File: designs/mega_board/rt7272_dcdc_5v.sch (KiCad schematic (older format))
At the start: 13 parts

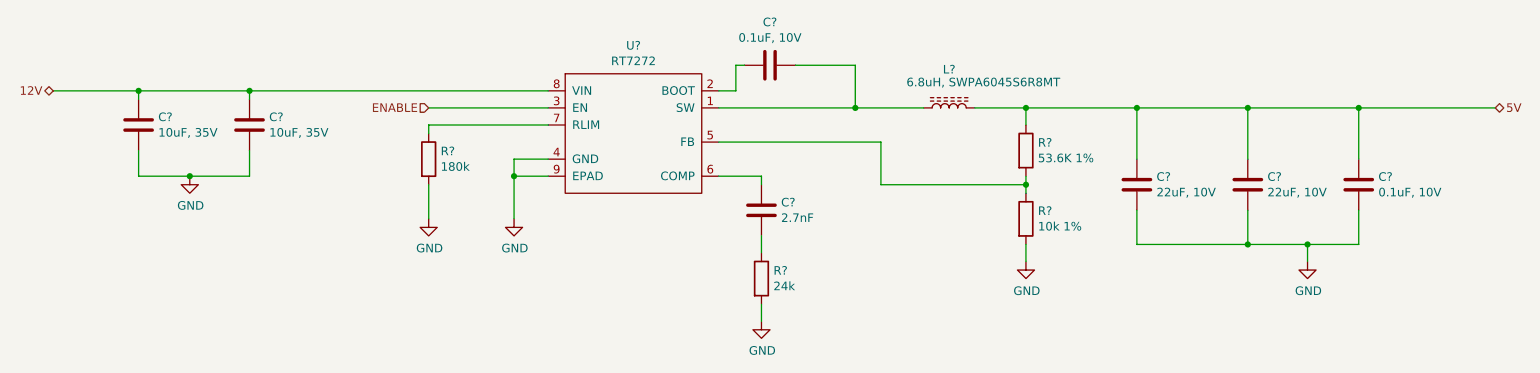
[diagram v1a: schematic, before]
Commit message: Enumerate components as is in eagle design.
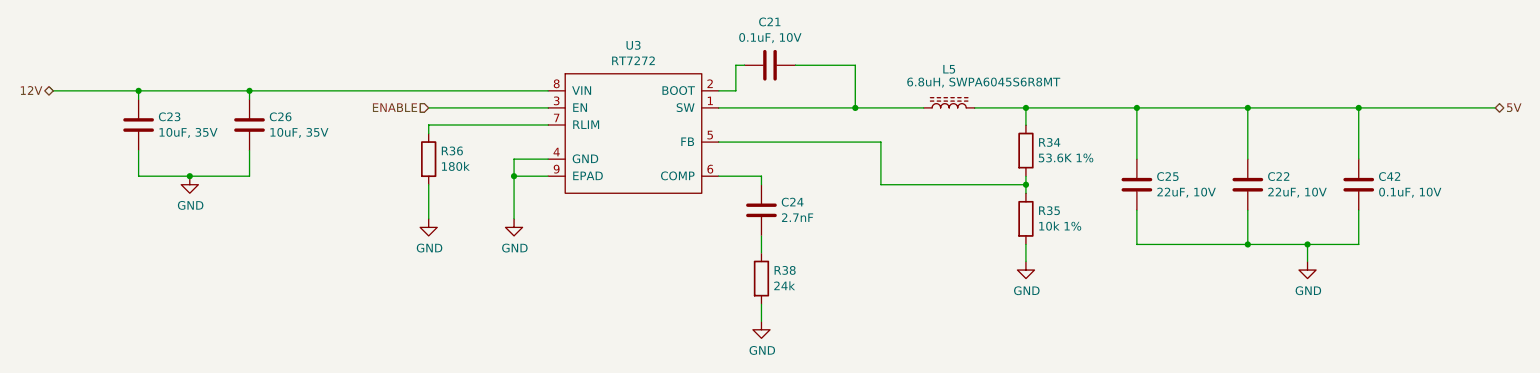
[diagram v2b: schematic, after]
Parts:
- C21, C24, C42: renamed from C?; footprint (none) -> LibreRouter_MegaBoard:C0402
- C22, C23, C25, C26: renamed from C?; footprint (none) -> LibreRouter_MegaBoard:C0805
- L5: renamed from L?; footprint (none) -> LibreRouter_MegaBoard:SWPA6028S
- R34, R35, R36, R38: renamed from R?; footprint (none) -> LibreRouter_MegaBoard:R0402
- U3: renamed from U?; footprint (none) -> LibreRouter_MegaBoard:RT8250-SOP8

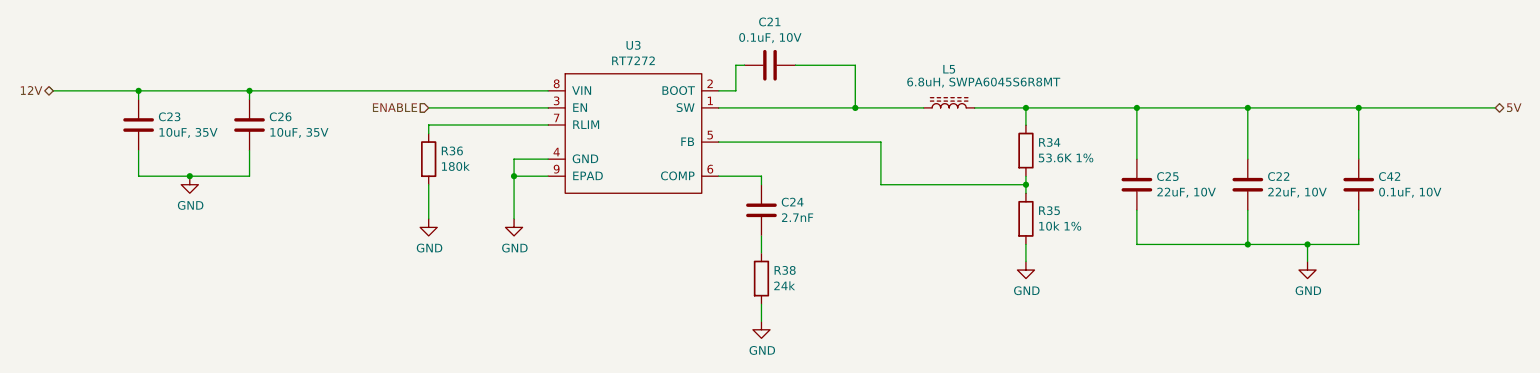
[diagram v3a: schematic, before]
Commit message: Add capacitor definito to BOM
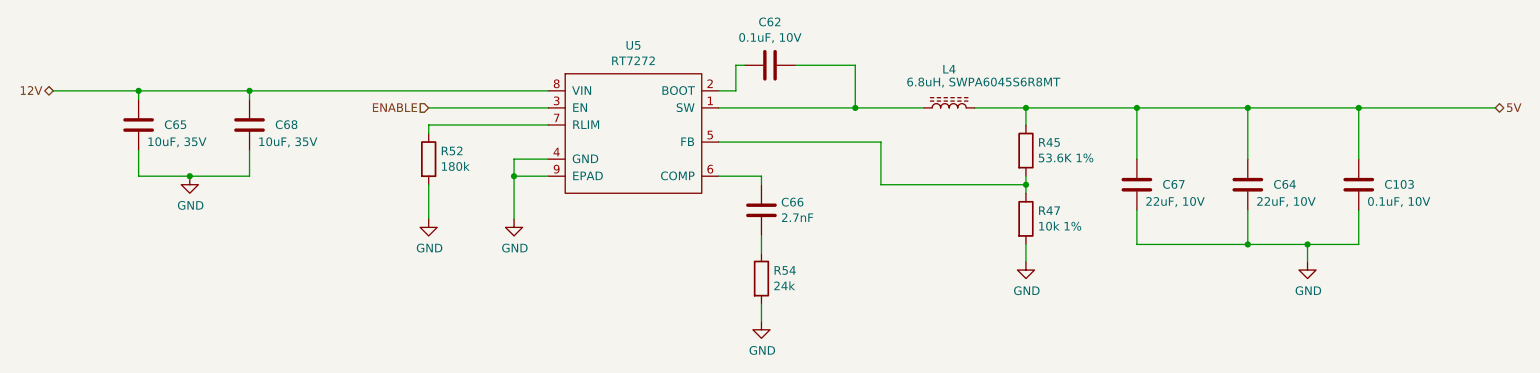
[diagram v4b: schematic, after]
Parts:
- C21, C42: Manufacturer (none) -> Murata Electronics; Manufacturer PN (none) -> GCM155R71A104KA55D; Supplier (none) -> DigiKey; Supplier PN (none) -> 490-16434-6-ND
- C22, C25: Manufacturer (none) -> Murata Electronics; Manufacturer PN (none) -> GRM21BR61A226ME51L; Supplier (none) -> DigiKey; Supplier PN (none) -> 490-10511-6-ND
- C23, C26: Manufacturer (none) -> Murata Electronics; Manufacturer PN (none) -> GRM21BR6YA106ME43L; Supplier (none) -> DigiKey; Supplier PN (none) -> 490-10515-6-ND
- C24: Manufacturer (none) -> Murata Electronics; Manufacturer PN (none) -> GRM1557U1A272JA01D; Supplier (none) -> DigiKey; Supplier PN (none) -> 490-6275-6-ND
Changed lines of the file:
@@
 $Descr A4 11693 8268
 encoding utf-8
-Sheet 7 14
+Sheet 9 14
 Title ""
 Date ""
@@
 AR Path="/5D0328DE/5D4FEB2F/5D42D1B4" Ref="U5"  Part="1"
 AR Path="/5D42D1B4" Ref="U?"  Part="1"
-F 0 "U3" H 5050 4115 50  0000 C CNN
+F 0 "U5" H 5050 4115 50  0000 C CNN
 F 1 "RT7272" H 5050 4024 50  0000 C CNN
 F 2 "LibreRouter_MegaBoard:RT8250-SOP8" H 5050 3600 50  0001 C CNN
@@
 AR Path="/5D0328DE/5D4FE12B/5D42D229" Ref="C53"  Part="1"
 AR Path="/5D0328DE/5D4FEB2F/5D42D229" Ref="C68"  Part="1"
-F 0 "C26" H 2915 3596 50  0000 L CNN
-F 1 "10uF, 35V" H 2915 3505 50  0000 L CNN
+F 0 "C68" H 2950 3550 50  0000 L CNN
+F 1 "10uF, 35V" H 2850 3450 50  0000 L CNN
 F 2 "LibreRouter_MegaBoard:C0805" H 2838 3400 50  0001 C CNN
 F 3 "~" H 2800 3550 50  0001 C CNN
+F 4 "DigiKey" H 2800 3550 50  0001 C CNN "Supplier"
+F 5 "Murata Electronics" H 2800 3550 50  0001 C CNN "Manufacturer"
+F 6 "GRM21BR6YA106ME43L" H 2800 3550 50  0001 C CNN "Manufacturer PN"
+F 7 "490-10515-6-ND" H 2800 3550 50  0001 C CNN "Supplier PN"
 	1    2800 3550
 	1    0    0    -1
@@
 AR Path="/5D0328DE/5D4FE12B/5D42D2DE" Ref="R13"  Part="1"
 AR Path="/5D0328DE/5D4FEB2F/5D42D2DE" Ref="R52"  Part="1"
-F 0 "R36" H 3920 3796 50  0000 L CNN
+F 0 "R52" H 3920 3796 50  0000 L CNN
 F 1 "180k" H 3920 3705 50  0000 L CNN
 F 2 "LibreRouter_MegaBoard:R0402" V 3780 3750 50  0001 C CNN
@@
 AR Path="/5D0328DE/5D4FE12B/5D42D3B9" Ref="L3"  Part="1"
 AR Path="/5D0328DE/5D4FEB2F/5D42D3B9" Ref="L4"  Part="1"
-F 0 "L5" V 7125 3450 50  0000 C CNN
+F 0 "L4" V 7125 3450 50  0000 C CNN
 F 1 "6.8uH, SWPA6045S6R8MT" V 7050 3250 50  0000 C CNN
 F 2 "LibreRouter_MegaBoard:SWPA6028S" H 6900 3450 50  0001 C CNN
@@
 AR Path="/5D0328DE/5D4FE12B/5D42D488" Ref="C30"  Part="1"
 AR Path="/5D0328DE/5D4FEB2F/5D42D488" Ref="C62"  Part="1"
-F 0 "C21" V 5598 3200 50  0000 C CNN
+F 0 "C62" V 5598 3200 50  0000 C CNN
 F 1 "0.1uF, 10V" V 5689 3200 50  0000 C CNN
 F 2 "LibreRouter_MegaBoard:C0402" H 5888 3050 50  0001 C CNN
 F 3 "~" H 5850 3200 50  0001 C CNN
+F 4 "Murata Electronics" H 5850 3200 50  0001 C CNN "Manufacturer"
+F 5 "GCM155R71A104KA55D" H 5850 3200 50  0001 C CNN "Manufacturer PN"
+F 6 "DigiKey" H 5850 3200 50  0001 C CNN "Supplier"
+F 7 "490-16434-6-ND" H 5850 3200 50  0001 C CNN "Supplier PN"
 	1    5850 3200
 	0    1    1    0
@@
 AR Path="/5D0328DE/5D4FE12B/5D42D571" Ref="R10"  Part="1"
 AR Path="/5D0328DE/5D4FEB2F/5D42D571" Ref="R45"  Part="1"
-F 0 "R34" H 7420 3746 50  0000 L CNN
+F 0 "R45" H 7420 3746 50  0000 L CNN
 F 1 "53.6K 1%" H 7420 3655 50  0000 L CNN
 F 2 "LibreRouter_MegaBoard:R0402" V 7280 3700 50  0001 C CNN
@@
 AR Path="/5D0328DE/5D4FE12B/5D42D5CB" Ref="R12"  Part="1"
 AR Path="/5D0328DE/5D4FEB2F/5D42D5CB" Ref="R47"  Part="1"
-F 0 "R35" H 7420 4146 50  0000 L CNN
+F 0 "R47" H 7420 4146 50  0000 L CNN
 F 1 "10k 1%" H 7420 4055 50  0000 L CNN
 F 2 "LibreRouter_MegaBoard:R0402" V 7280 4100 50  0001 C CNN
@@
 AR Path="/5D0328DE/5D4FE12B/5D42D605" Ref="R16"  Part="1"
 AR Path="/5D0328DE/5D4FEB2F/5D42D605" Ref="R54"  Part="1"
-F 0 "R38" H 5870 4496 50  0000 L CNN
+F 0 "R54" H 5870 4496 50  0000 L CNN
 F 1 "24k" H 5870 4405 50  0000 L CNN
 F 2 "LibreRouter_MegaBoard:R0402" V 5730 4450 50  0001 C CNN
@@
 AR Path="/5D0328DE/5D4FE12B/5D42D659" Ref="C45"  Part="1"
 AR Path="/5D0328DE/5D4FEB2F/5D42D659" Ref="C66"  Part="1"
-F 0 "C24" H 5685 4004 50  0000 R CNN
+F 0 "C66" H 5685 4004 50  0000 R CNN
 F 1 "2.7nF" H 5685 4095 50  0000 R CNN
 F 2 "LibreRouter_MegaBoard:C0402" H 5838 3900 50  0001 C CNN
 F 3 "~" H 5800 4050 50  0001 C CNN
+F 4 "DigiKey" H 5800 4050 50  0001 C CNN "Supplier"
+F 5 "GRM1557U1A272JA01D" H 5800 4050 50  0001 C CNN "Manufacturer PN"
+F 6 "490-6275-6-ND" H 5800 4050 50  0001 C CNN "Supplier PN"
+F 7 "Murata Electronics" H 5800 4050 50  0001 C CNN "Manufacturer"
 	1    5800 4050
 	-1   0    0    1
@@
 AR Path="/5D0328DE/5D4FE12B/5D42DAC0" Ref="C46"  Part="1"
 AR Path="/5D0328DE/5D4FEB2F/5D42DAC0" Ref="C67"  Part="1"
-F 0 "C25" H 7885 3854 50  0000 R CNN
-F 1 "22uF, 10V" H 7885 3945 50  0000 R CNN
+F 0 "C67" H 7850 3900 50  0000 R CNN
+F 1 "22uF, 10V" H 7950 4000 50  0000 R CNN
 F 2 "LibreRouter_MegaBoard:C0805" H 8038 3750 50  0001 C CNN
 F 3 "~" H 8000 3900 50  0001 C CNN
+F 4 "DigiKey" H 8000 3900 50  0001 C CNN "Supplier"
+F 5 "GRM21BR61A226ME51L" H 8000 3900 50  0001 C CNN "Manufacturer PN"
+F 6 "490-10511-6-ND" H 8000 3900 50  0001 C CNN "Supplier PN"
+F 7 "Murata Electronics" H 8000 3900 50  0001 C CNN "Manufacturer"
 	1    8000 3900
 	-1   0    0    1
@@
 AR Path="/5D0328DE/5D4FE12B/5D42DBCD" Ref="C31"  Part="1"
 AR Path="/5D0328DE/5D4FEB2F/5D42DBCD" Ref="C64"  Part="1"
-F 0 "C22" H 8535 3854 50  0000 R CNN
-F 1 "22uF, 10V" H 8535 3945 50  0000 R CNN
+F 0 "C64" H 8500 3900 50  0000 R CNN
+F 1 "22uF, 10V" H 8600 4000 50  0000 R CNN
 F 2 "LibreRouter_MegaBoard:C0805" H 8688 3750 50  0001 C CNN
 F 3 "~" H 8650 3900 50  0001 C CNN
+F 4 "DigiKey" H 8650 3900 50  0001 C CNN "Supplier"
+F 5 "GRM21BR61A226ME51L" H 8650 3900 50  0001 C CNN "Manufacturer PN"
+F 6 "490-10511-6-ND" H 8650 3900 50  0001 C CNN "Supplier PN"
+F 7 "Murata Electronics" H 8650 3900 50  0001 C CNN "Manufacturer"
 	1    8650 3900
 	-1   0    0    1
@@
 AR Path="/5D0328DE/5D4FE12B/5D42DC2B" Ref="C102"  Part="1"
 AR Path="/5D0328DE/5D4FEB2F/5D42DC2B" Ref="C103"  Part="1"
-F 0 "C42" H 9185 3854 50  0000 R CNN
-F 1 "0.1uF, 10V" H 9185 3945 50  0000 R CNN
+F 0 "C103" H 9150 3900 50  0000 R CNN
+F 1 "0.1uF, 10V" H 9250 4000 50  0000 R CNN
 F 2 "LibreRouter_MegaBoard:C0402" H 9338 3750 50  0001 C CNN
 F 3 "~" H 9300 3900 50  0001 C CNN
+F 4 "Murata Electronics" H 9300 3900 50  0001 C CNN "Manufacturer"
+F 5 "GCM155R71A104KA55D" H 9300 3900 50  0001 C CNN "Manufacturer PN"
+F 6 "DigiKey" H 9300 3900 50  0001 C CNN "Supplier"
+F 7 "490-16434-6-ND" H 9300 3900 50  0001 C CNN "Supplier PN"
 	1    9300 3900
 	-1   0    0    1
@@
 AR Path="/5D0328DE/5D4FE12B/5D43058C" Ref="C44"  Part="1"
 AR Path="/5D0328DE/5D4FEB2F/5D43058C" Ref="C65"  Part="1"
-F 0 "C23" H 2265 3596 50  0000 L CNN
-F 1 "10uF, 35V" H 2265 3505 50  0000 L CNN
+F 0 "C65" H 2300 3550 50  0000 L CNN
+F 1 "10uF, 35V" H 2200 3450 50  0000 L CNN
 F 2 "LibreRouter_MegaBoard:C0805" H 2188 3400 50  0001 C CNN
 F 3 "~" H 2150 3550 50  0001 C CNN
+F 4 "DigiKey" H 2150 3550 50  0001 C CNN "Supplier"
+F 5 "Murata Electronics" H 2150 3550 50  0001 C CNN "Manufacturer"
+F 6 "GRM21BR6YA106ME43L" H 2150 3550 50  0001 C CNN "Manufacturer PN"
+F 7 "490-10515-6-ND" H 2150 3550 50  0001 C CNN "Supplier PN"
 	1    2150 3550
 	1    0    0    -1

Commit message: Add BOM definition to all resistors
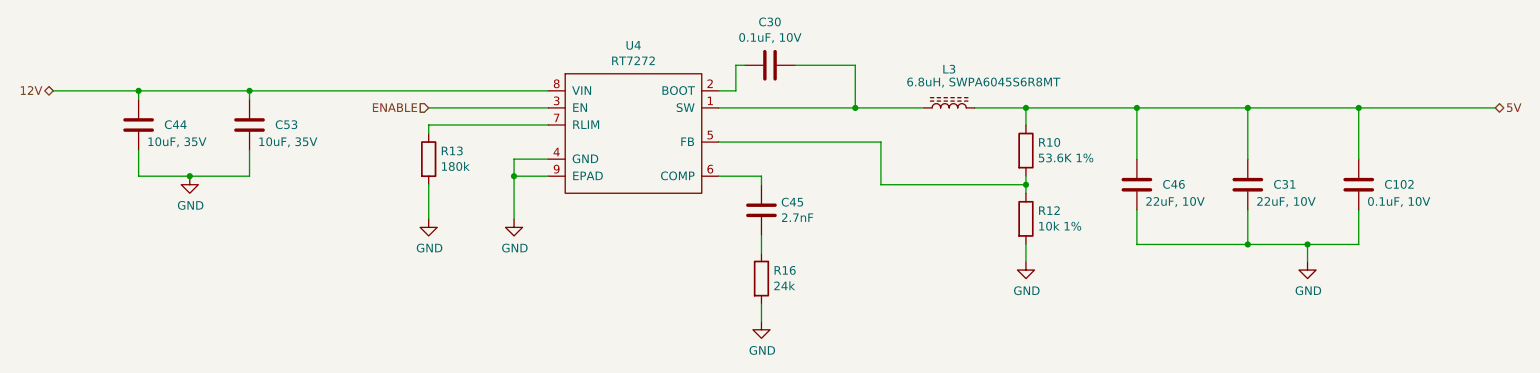
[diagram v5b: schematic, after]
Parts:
- R34: Manufacturer (none) -> Panasonic Electronic Components; Manufacturer PN (none) -> ERJ-2RKF5362X; Supplier (none) -> DigiKey; Supplier PN (none) -> P53.6KLDKR-ND
- R35: Manufacturer (none) -> Panasonic Electronic Components; Manufacturer PN (none) -> ERJ-PA2F1002X; Supplier (none) -> DigiKey; Supplier PN (none) -> P17230DKR-ND
- R36: Manufacturer (none) -> Panasonic Electronic Components; Manufacturer PN (none) -> ERJ-PA2F1803X; Supplier (none) -> DigiKey; Supplier PN (none) -> P124450DKR-ND
- R38: Manufacturer (none) -> Panasonic Electronic Components; Manufacturer PN (none) -> ERJ-PA2F2402X; Supplier (none) -> DigiKey; Supplier PN (none) -> P124459DKR-ND
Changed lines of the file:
@@
 $Descr A4 11693 8268
 encoding utf-8
-Sheet 9 14
+Sheet 8 14
 Title ""
 Date ""
@@
 AR Path="/5D0328DE/5D4FEB2F/5D42D1B4" Ref="U5"  Part="1"
 AR Path="/5D42D1B4" Ref="U?"  Part="1"
-F 0 "U5" H 5050 4115 50  0000 C CNN
+F 0 "U4" H 5050 4115 50  0000 C CNN
 F 1 "RT7272" H 5050 4024 50  0000 C CNN
 F 2 "LibreRouter_MegaBoard:RT8250-SOP8" H 5050 3600 50  0001 C CNN
@@
 AR Path="/5D0328DE/5D4FE12B/5D42D229" Ref="C53"  Part="1"
 AR Path="/5D0328DE/5D4FEB2F/5D42D229" Ref="C68"  Part="1"
-F 0 "C68" H 2950 3550 50  0000 L CNN
+F 0 "C53" H 2950 3550 50  0000 L CNN
 F 1 "10uF, 35V" H 2850 3450 50  0000 L CNN
 F 2 "LibreRouter_MegaBoard:C0805" H 2838 3400 50  0001 C CNN
@@
 AR Path="/5D0328DE/5D4FE12B/5D42D2DE" Ref="R13"  Part="1"
 AR Path="/5D0328DE/5D4FEB2F/5D42D2DE" Ref="R52"  Part="1"
-F 0 "R52" H 3920 3796 50  0000 L CNN
+F 0 "R13" H 3920 3796 50  0000 L CNN
 F 1 "180k" H 3920 3705 50  0000 L CNN
 F 2 "LibreRouter_MegaBoard:R0402" V 3780 3750 50  0001 C CNN
 F 3 "~" H 3850 3750 50  0001 C CNN
+F 4 "Panasonic Electronic Components" H 3850 3750 50  0001 C CNN "Manufacturer"
+F 5 "ERJ-PA2F1803X" H 3850 3750 50  0001 C CNN "Manufacturer PN"
+F 6 "DigiKey" H 3850 3750 50  0001 C CNN "Supplier"
+F 7 "P124450DKR-ND" H 3850 3750 50  0001 C CNN "Supplier PN"
 	1    3850 3750
 	1    0    0    -1
@@
 AR Path="/5D0328DE/5D4FE12B/5D42D3B9" Ref="L3"  Part="1"
 AR Path="/5D0328DE/5D4FEB2F/5D42D3B9" Ref="L4"  Part="1"
-F 0 "L4" V 7125 3450 50  0000 C CNN
+F 0 "L3" V 7125 3450 50  0000 C CNN
 F 1 "6.8uH, SWPA6045S6R8MT" V 7050 3250 50  0000 C CNN
 F 2 "LibreRouter_MegaBoard:SWPA6028S" H 6900 3450 50  0001 C CNN
@@
 AR Path="/5D0328DE/5D4FE12B/5D42D488" Ref="C30"  Part="1"
 AR Path="/5D0328DE/5D4FEB2F/5D42D488" Ref="C62"  Part="1"
-F 0 "C62" V 5598 3200 50  0000 C CNN
+F 0 "C30" V 5598 3200 50  0000 C CNN
 F 1 "0.1uF, 10V" V 5689 3200 50  0000 C CNN
 F 2 "LibreRouter_MegaBoard:C0402" H 5888 3050 50  0001 C CNN
@@
 AR Path="/5D0328DE/5D4FE12B/5D42D571" Ref="R10"  Part="1"
 AR Path="/5D0328DE/5D4FEB2F/5D42D571" Ref="R45"  Part="1"
-F 0 "R45" H 7420 3746 50  0000 L CNN
+F 0 "R10" H 7420 3746 50  0000 L CNN
 F 1 "53.6K 1%" H 7420 3655 50  0000 L CNN
 F 2 "LibreRouter_MegaBoard:R0402" V 7280 3700 50  0001 C CNN
 F 3 "~" H 7350 3700 50  0001 C CNN
+F 4 "Panasonic Electronic Components" H 7350 3700 50  0001 C CNN "Manufacturer"
+F 5 "ERJ-2RKF5362X" H 7350 3700 50  0001 C CNN "Manufacturer PN"
+F 6 "DigiKey" H 7350 3700 50  0001 C CNN "Supplier"
+F 7 "P53.6KLDKR-ND" H 7350 3700 50  0001 C CNN "Supplier PN"
 	1    7350 3700
 	1    0    0    -1
@@
 AR Path="/5D0328DE/5D4FE12B/5D42D5CB" Ref="R12"  Part="1"
 AR Path="/5D0328DE/5D4FEB2F/5D42D5CB" Ref="R47"  Part="1"
-F 0 "R47" H 7420 4146 50  0000 L CNN
+F 0 "R12" H 7420 4146 50  0000 L CNN
 F 1 "10k 1%" H 7420 4055 50  0000 L CNN
 F 2 "LibreRouter_MegaBoard:R0402" V 7280 4100 50  0001 C CNN
 F 3 "~" H 7350 4100 50  0001 C CNN
+F 4 "Panasonic Electronic Components" H 7350 4100 50  0001 C CNN "Manufacturer"
+F 5 "ERJ-PA2F1002X" H 7350 4100 50  0001 C CNN "Manufacturer PN"
+F 6 "DigiKey" H 7350 4100 50  0001 C CNN "Supplier"
+F 7 "P17230DKR-ND" H 7350 4100 50  0001 C CNN "Supplier PN"
 	1    7350 4100
 	1    0    0    -1
@@
 AR Path="/5D0328DE/5D4FE12B/5D42D605" Ref="R16"  Part="1"
 AR Path="/5D0328DE/5D4FEB2F/5D42D605" Ref="R54"  Part="1"
-F 0 "R54" H 5870 4496 50  0000 L CNN
+F 0 "R16" H 5870 4496 50  0000 L CNN
 F 1 "24k" H 5870 4405 50  0000 L CNN
 F 2 "LibreRouter_MegaBoard:R0402" V 5730 4450 50  0001 C CNN
 F 3 "~" H 5800 4450 50  0001 C CNN
+F 4 "Panasonic Electronic Components" H 5800 4450 50  0001 C CNN "Manufacturer"
+F 5 "ERJ-PA2F2402X" H 5800 4450 50  0001 C CNN "Manufacturer PN"
+F 6 "DigiKey" H 5800 4450 50  0001 C CNN "Supplier"
+F 7 "P124459DKR-ND" H 5800 4450 50  0001 C CNN "Supplier PN"
 	1    5800 4450
 	1    0    0    -1
@@
 AR Path="/5D0328DE/5D4FE12B/5D42D659" Ref="C45"  Part="1"
 AR Path="/5D0328DE/5D4FEB2F/5D42D659" Ref="C66"  Part="1"
-F 0 "C66" H 5685 4004 50  0000 R CNN
+F 0 "C45" H 5685 4004 50  0000 R CNN
 F 1 "2.7nF" H 5685 4095 50  0000 R CNN
 F 2 "LibreRouter_MegaBoard:C0402" H 5838 3900 50  0001 C CNN
@@
 AR Path="/5D0328DE/5D4FE12B/5D42DAC0" Ref="C46"  Part="1"
 AR Path="/5D0328DE/5D4FEB2F/5D42DAC0" Ref="C67"  Part="1"
-F 0 "C67" H 7850 3900 50  0000 R CNN
+F 0 "C46" H 7850 3900 50  0000 R CNN
 F 1 "22uF, 10V" H 7950 4000 50  0000 R CNN
 F 2 "LibreRouter_MegaBoard:C0805" H 8038 3750 50  0001 C CNN
@@
 AR Path="/5D0328DE/5D4FE12B/5D42DBCD" Ref="C31"  Part="1"
 AR Path="/5D0328DE/5D4FEB2F/5D42DBCD" Ref="C64"  Part="1"
-F 0 "C64" H 8500 3900 50  0000 R CNN
+F 0 "C31" H 8500 3900 50  0000 R CNN
 F 1 "22uF, 10V" H 8600 4000 50  0000 R CNN
 F 2 "LibreRouter_MegaBoard:C0805" H 8688 3750 50  0001 C CNN
@@
 AR Path="/5D0328DE/5D4FE12B/5D42DC2B" Ref="C102"  Part="1"
 AR Path="/5D0328DE/5D4FEB2F/5D42DC2B" Ref="C103"  Part="1"
-F 0 "C103" H 9150 3900 50  0000 R CNN
+F 0 "C102" H 9150 3900 50  0000 R CNN
 F 1 "0.1uF, 10V" H 9250 4000 50  0000 R CNN
 F 2 "LibreRouter_MegaBoard:C0402" H 9338 3750 50  0001 C CNN
@@
 AR Path="/5D0328DE/5D4FE12B/5D42DD90" Ref="#PWR0157"  Part="1"
 AR Path="/5D0328DE/5D4FEB2F/5D42DD90" Ref="#PWR0163"  Part="1"
-F 0 "#PWR0163" H 7350 4100 50  0001 C CNN
+F 0 "#PWR0157" H 7350 4100 50  0001 C CNN
 F 1 "GND" H 7355 4177 50  0000 C CNN
 F 2 "" H 7350 4350 50  0001 C CNN
@@
 AR Path="/5D0328DE/5D4FE12B/5D42DDBC" Ref="#PWR0158"  Part="1"
 AR Path="/5D0328DE/5D4FEB2F/5D42DDBC" Ref="#PWR0164"  Part="1"
-F 0 "#PWR0164" H 9000 4100 50  0001 C CNN
+F 0 "#PWR0158" H 9000 4100 50  0001 C CNN
 F 1 "GND" H 9005 4177 50  0000 C CNN
 F 2 "" H 9000 4350 50  0001 C CNN
@@
 AR Path="/5D0328DE/5D4FE12B/5D42FF27" Ref="#PWR0159"  Part="1"
 AR Path="/5D0328DE/5D4FEB2F/5D42FF27" Ref="#PWR0165"  Part="1"
-F 0 "#PWR0165" H 5800 4450 50  0001 C CNN
+F 0 "#PWR0159" H 5800 4450 50  0001 C CNN
 F 1 "GND" H 5805 4527 50  0000 C CNN
 F 2 "" H 5800 4700 50  0001 C CNN
@@
 AR Path="/5D0328DE/5D4FE12B/5D43058C" Ref="C44"  Part="1"
 AR Path="/5D0328DE/5D4FEB2F/5D43058C" Ref="C65"  Part="1"
-F 0 "C65" H 2300 3550 50  0000 L CNN
+F 0 "C44" H 2300 3550 50  0000 L CNN
 F 1 "10uF, 35V" H 2200 3450 50  0000 L CNN
 F 2 "LibreRouter_MegaBoard:C0805" H 2188 3400 50  0001 C CNN
@@
 AR Path="/5D0328DE/5D4FE12B/5D4322E2" Ref="#PWR0160"  Part="1"
 AR Path="/5D0328DE/5D4FEB2F/5D4322E2" Ref="#PWR0166"  Part="1"
-F 0 "#PWR0166" H 2450 3600 50  0001 C CNN
+F 0 "#PWR0160" H 2450 3600 50  0001 C CNN
 F 1 "GND" H 2455 3677 50  0000 C CNN
 F 2 "" H 2450 3850 50  0001 C CNN
@@
 AR Path="/5D0328DE/5D4FE12B/5D4323C5" Ref="#PWR0161"  Part="1"
 AR Path="/5D0328DE/5D4FEB2F/5D4323C5" Ref="#PWR0167"  Part="1"
-F 0 "#PWR0167" H 3850 3850 50  0001 C CNN
+F 0 "#PWR0161" H 3850 3850 50  0001 C CNN
 F 1 "GND" H 3855 3927 50  0000 C CNN
 F 2 "" H 3850 4100 50  0001 C CNN
@@
 AR Path="/5D0328DE/5D4FE12B/5D4323EC" Ref="#PWR0162"  Part="1"
 AR Path="/5D0328DE/5D4FEB2F/5D4323EC" Ref="#PWR0168"  Part="1"
-F 0 "#PWR0168" H 4350 3850 50  0001 C CNN
+F 0 "#PWR0162" H 4350 3850 50  0001 C CNN
 F 1 "GND" H 4355 3927 50  0000 C CNN
 F 2 "" H 4350 4100 50  0001 C CNN

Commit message: Add BOM definition for components. We need more iformation for all the components that are not defined.
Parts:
- L5: Manufacturer (none) -> Abracon LLC; Manufacturer PN (none) -> ASPI-6045S-6R8M-T; Supplier (none) -> DigiKey; Supplier PN (none) -> 535-13046-6-ND
- U3: Manufacturer (none) -> Richtek USA Inc.; Manufacturer PN (none) -> RT7272AGSP; Supplier (none) -> DigiKey; Supplier PN (none) -> RT7272AGSPDKR-ND
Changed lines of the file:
@@
 F 2 "LibreRouter_MegaBoard:RT8250-SOP8" H 5050 3600 50  0001 C CNN
 F 3 "" H 5050 3600 50  0001 C CNN
+F 4 "Richtek USA Inc." H 5050 3600 50  0001 C CNN "Manufacturer"
+F 5 "RT7272AGSP" H 5050 3600 50  0001 C CNN "Manufacturer PN"
+F 6 "DigiKey" H 5050 3600 50  0001 C CNN "Supplier"
+F 7 "RT7272AGSPDKR-ND" H 5050 3600 50  0001 C CNN "Supplier PN"
 	1    5050 3600
 	1    0    0    -1
@@
 F 2 "LibreRouter_MegaBoard:SWPA6028S" H 6900 3450 50  0001 C CNN
 F 3 "~" H 6900 3450 50  0001 C CNN
+F 4 "Abracon LLC" H 6900 3450 50  0001 C CNN "Manufacturer"
+F 5 "ASPI-6045S-6R8M-T" H 6900 3450 50  0001 C CNN "Manufacturer PN"
+F 6 "DigiKey" H 6900 3450 50  0001 C CNN "Supplier"
+F 7 "535-13046-6-ND" H 6900 3450 50  0001 C CNN "Supplier PN"
 	1    6900 3450
 	0    -1   -1   0
